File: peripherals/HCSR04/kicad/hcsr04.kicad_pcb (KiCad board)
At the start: 2 copper layers, 53.3 x 38.1 mm, 12 parts

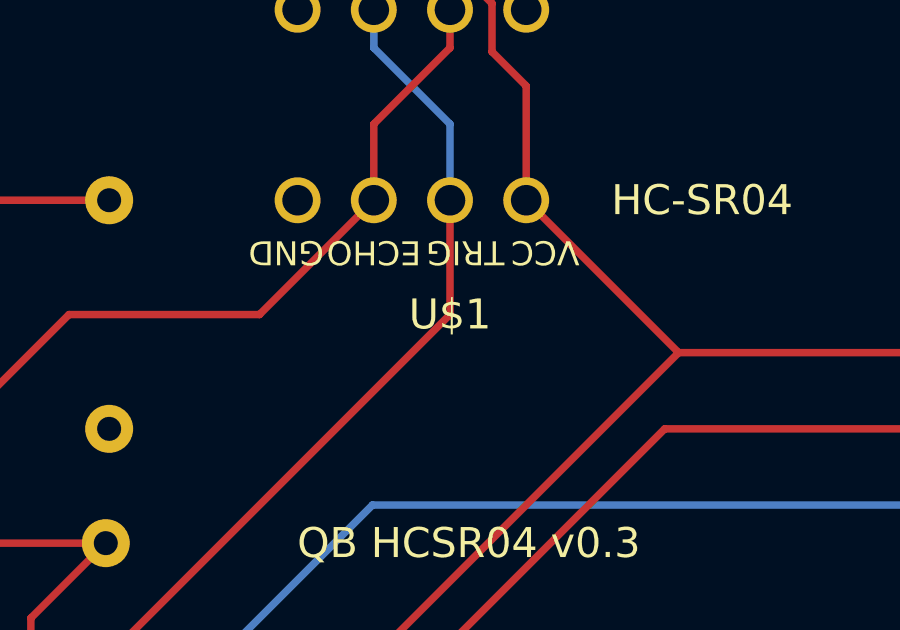
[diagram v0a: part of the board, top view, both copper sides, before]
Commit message: Adding README for HC-SR04
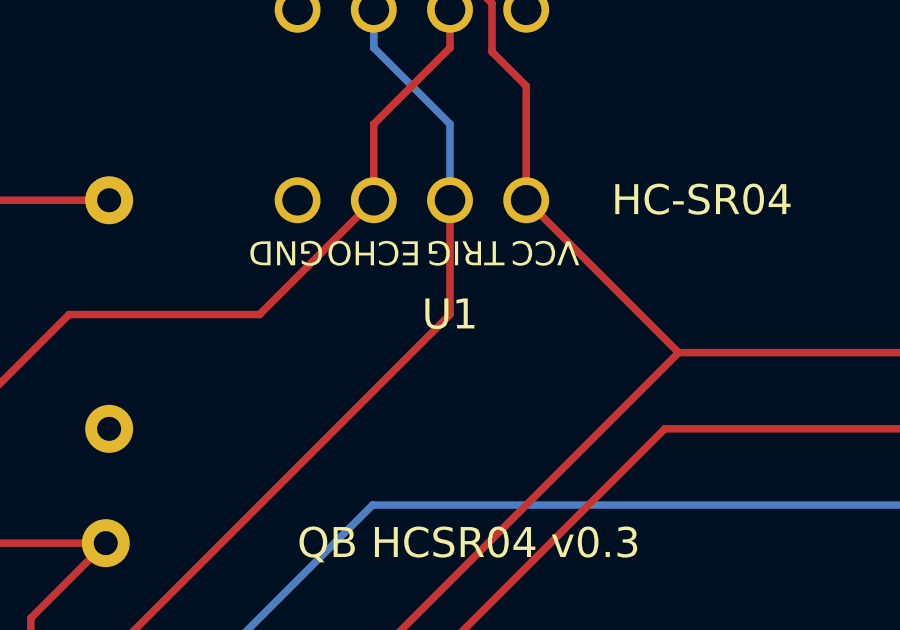
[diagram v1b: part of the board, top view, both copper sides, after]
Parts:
- renumbered U$1 to U1, U$2 to U2
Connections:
- JP1 pad 14: /PIO2 -> /PIO1
- R1 pad 2: /PIO2 -> /PIO1
- R2 pad 1: /PIO2 -> /PIO1
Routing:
- net /PIO1: track 43.2 -> 72.2 mm
- net /PIO2: track 29.1 -> 0.00 mm
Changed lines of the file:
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@@
 	(net 12 "unconnected-(JP1-Pad2)")
 	(net 13 "/PIO4")
-	(net 14 "/PIO2")
+	(net 14 "Net-(U1-ECHO)")
 	(net 15 "/PIO3")
 	(net 16 "Net-(JP2-Pad3)")
@@
 	(net 19 "unconnected-(JP5-Pad1)")
 	(net 20 "unconnected-(JP6-Pad1)")
-	(net 21 "Net-(U$1-ECHO)")
 	(footprint "Connector_PinHeader_2.54mm:PinHeader_1x15_P2.54mm_Horizontal"
 		(layer "F.Cu")
@@
 			)
 		)
-		(sheetname "Root")
+		(sheetname "/")
 		(sheetfile "hcsr04.kicad_sch")
 		(attr through_hole)
@@
 			(layers "*.Cu" "*.Mask")
 			(remove_unused_layers no)
-			(net 14 "/PIO2")
+			(net 11 "/PIO1")
 			(pinfunction "14")
 			(pintype "passive")
@@
 			)
 		)
-		(sheetname "Root")
+		(sheetname "/")
 		(sheetfile "hcsr04.kicad_sch")
 		(attr through_hole)
@@
 		(layer "F.Cu")
 		(at 148.5011 96.1136 180)
-		(property "Reference" "U$1"
+		(property "Reference" "U1"
 			(at -1.27 -3.81 180)
 			(layer "F.SilkS")
@@
 			)
 		)
-		(sheetname "Root")
+		(sheetname "/")
 		(sheetfile "hcsr04.kicad_sch")
 		(attr through_hole)
@@
 			(layers "*.Cu" "*.Mask")
 			(remove_unused_layers no)
-			(net 21 "Net-(U$1-ECHO)")
+			(net 14 "Net-(U1-ECHO)")
 			(pinfunction "ECHO")
 			(pintype "bidirectional")
@@
 			)
 		)
-		(sheetname "Root")
+		(sheetname "/")
 		(sheetfile "hcsr04.kicad_sch")
 		(attr through_hole)
@@
 			)
 		)
-		(sheetname "Root")
+		(sheetname "/")
 		(sheetfile "hcsr04.kicad_sch")
 		(attr through_hole)
@@
 			)
 		)
-		(sheetname "Root")
+		(sheetname "/")
 		(sheetfile "hcsr04.kicad_sch")
 		(attr through_hole)
@@
 			)
 		)
-		(sheetname "Root")
+		(sheetname "/")
 		(sheetfile "hcsr04.kicad_sch")
 		(attr through_hole)
@@
 			(layers "*.Cu" "*.Mask")
 			(remove_unused_layers no)
-			(net 21 "Net-(U$1-ECHO)")
+			(net 14 "Net-(U1-ECHO)")
 			(pinfunction "1")
 			(pintype "passive")
@@
 			(layers "*.Cu" "*.Mask")
 			(remove_unused_layers no)
-			(net 14 "/PIO2")
+			(net 11 "/PIO1")
 			(pinfunction "2")
 			(pintype "passive")
@@
 		(layer "B.Cu")
 		(at 148.5011 89.7636)
-		(property "Reference" "U$2"
+		(property "Reference" "U2"
 			(at -1.27 -2.54 180)
 			(layer "B.SilkS")
@@
 			)
 		)
-		(sheetname "Root")
+		(sheetname "/")
 		(sheetfile "hcsr04.kicad_sch")
 		(attr through_hole)
@@
 			(layers "*.Cu" "*.Mask")
 			(remove_unused_layers no)
-			(net 21 "Net-(U$1-ECHO)")
+			(net 14 "Net-(U1-ECHO)")
 			(pinfunction "ECHO")
 			(pintype "bidirectional")
@@
 			)
 		)
-		(sheetname "Root")
+		(sheetname "/")
 		(sheetfile "hcsr04.kicad_sch")
 		(attr through_hole)
@@
 			(layers "*.Cu" "*.Mask")
 			(remove_unused_layers no)
-			(net 14 "/PIO2")
+			(net 11 "/PIO1")
 			(pinfunction "1")
 			(pintype "passive")
@@
 			)
 		)
-		(sheetname "Root")
+		(sheetname "/")
 		(sheetfile "hcsr04.kicad_sch")
 		(attr through_hole)
@@
 			)
 		)
-		(sheetname "Root")
+		(sheetname "/")
 		(sheetfile "hcsr04.kicad_sch")
 		(attr through_hole)
@@
 			)
 		)
-		(sheetname "Root")
+		(sheetname "/")
 		(sheetfile "hcsr04.kicad_sch")
 		(attr through_hole)
@@
 	)
 	(segment
+		(start 133.2611 96.1136)
+		(end 138.4091 96.1136)
+		(width 0.25)
+		(layer "F.Cu")
+		(net 11)
+	)
+	(segment
 		(start 136.308512 120.1986)
 		(end 137.0711 119.436012)
@@
 	)
 	(segment
+		(start 131.9911 117.7036)
+		(end 131.9911 97.3836)
+		(width 0.25)
+		(layer "F.Cu")
+		(net 11)
+	)
+	(segment
 		(start 137.0711 119.436012)
 		(end 137.0711 112.6236)
@@
 	)
 	(segment
+		(start 133.2611 118.9736)
+		(end 131.9911 117.7036)
+		(width 0.25)
+		(layer "F.Cu")
+		(net 11)
+	)
+	(segment
+		(start 131.9911 97.3836)
+		(end 133.2611 96.1136)
+		(width 0.25)
+		(layer "F.Cu")
+		(net 11)
+	)
+	(segment
 		(start 131.9461 120.1986)
 		(end 136.308512 120.1986)
@@
 	)
 	(segment
-		(start 133.2611 96.1136)
-		(end 138.4091 96.1136)
+		(start 147.2311 93.5736)
+		(end 149.7711 91.0336)
 		(width 0.25)
 		(layer "F.Cu")
@@
 	)
 	(segment
-		(start 131.9911 117.7036)
-		(end 131.9911 97.3836)
+		(start 149.7711 91.0336)
+		(end 149.7711 89.7636)
 		(width 0.25)
 		(layer "F.Cu")
@@
 	)
 	(segment
-		(start 133.2611 118.9736)
-		(end 131.9911 117.7036)
+		(start 133.2611 103.7336)
+		(end 137.0711 99.9236)
 		(width 0.25)
 		(layer "F.Cu")
@@
 	)
 	(segment
-		(start 131.9911 97.3836)
-		(end 133.2611 96.1136)
+		(start 147.2311 96.1136)
+		(end 147.2311 93.5736)
+		(width 0.25)
+		(layer "F.Cu")
+		(net 14)
+	)
+	(segment
+		(start 137.0711 99.9236)
+		(end 143.4211 99.9236)
+		(width 0.25)
+		(layer "F.Cu")
+		(net 14)
+	)
+	(segment
+		(start 143.4211 99.9236)
+		(end 147.2311 96.1136)
 		(width 0.25)
 		(layer "F.Cu")
@@
 		(net 16)
 	)
-	(segment
-		(start 147.2311 93.5736)
-		(end 149.7711 91.0336)
-		(width 0.25)
-		(layer "F.Cu")
-		(net 21)
-	)
-	(segment
-		(start 149.7711 91.0336)
-		(end 149.7711 89.7636)
-		(width 0.25)
-		(layer "F.Cu")
-		(net 21)
-	)
-	(segment
-		(start 133.2611 103.7336)
-		(end 137.0711 99.9236)
-		(width 0.25)
-		(layer "F.Cu")
-		(net 21)
-	)
-	(segment
-		(start 147.2311 96.1136)
-		(end 147.2311 93.5736)
-		(width 0.25)
-		(layer "F.Cu")
-		(net 21)
-	)
-	(segment
-		(start 137.0711 99.9236)
-		(end 143.4211 99.9236)
-		(width 0.25)
-		(layer "F.Cu")
-		(net 21)
-	)
-	(segment
-		(start 143.4211 99.9236)
-		(end 147.2311 96.1136)
-		(width 0.25)
-		(layer "F.Cu")
-		(net 21)
-	)
 	(zone
